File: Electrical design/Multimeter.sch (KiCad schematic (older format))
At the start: 31 parts

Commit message: Updated schematics.
Added speaker / buzzer, reset circuit (battery under-voltage lockout), changed battery charger IC.
Altered Vout circuit.
Added most resistor / capacitor values (those missing are either dependent on battery thermistor or ADC).
Updated to show "correct" op-amps.
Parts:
- removed C? (x7): CP1, symbol CP1
- removed Q?: Q_NMOS_DGS, symbol Q_NMOS_DGS
- removed Q?: Q_PMOS_DGS, symbol Q_PMOS_DGS
- added C106, C116, C119: 1u, my footprints:SMDuniversal_0603to1210_HandSoldering, symbol C
- added C108: 0.1u, my footprints:SMDuniversal_0603to1210_HandSoldering, symbol C
- added C109, C120, C121: 10u, my footprints:SMDuniversal_0603to1210_HandSoldering, symbol C
- added C112, C113, C118: 0.01u, my footprints:SMDuniversal_0603to1210_HandSoldering, symbol C
- added Q101: Q_PMOS_GSD, TO_SOT_Packages_SMD:SOT-23, symbol Q_PMOS_GSD
- added Q102: Q_NMOS_GSD, TO_SOT_Packages_SMD:SOT-23, symbol Q_NMOS_GSD
- added SP101: SPEAKER, Pin_Headers:Pin_Header_Straight_1x02, symbol SPEAKER
- added U103: BD4835, my footprints:VSOF5_HandSoldering, symbol BD4835
- C101, C102: renamed from C?; value C -> 18p; footprint (none) -> my footprints:SMDuniversal_0603to1210_HandSoldering
- C103, C104, C105: renamed from C?; value C -> 0.22u; footprint (none) -> my footprints:SMDuniversal_0603to1210_HandSoldering
- C107: renamed from C?; value C -> 1u; footprint (none) -> my footprints:SMDuniversal_0603to1210_HandSoldering
- C110, C117: renamed from C?; value C -> 0.1u; footprint (none) -> my footprints:SMDuniversal_0603to1210_HandSoldering
- C111: renamed from C?; value C -> 0.01u; footprint (none) -> my footprints:SMDuniversal_0603to1210_HandSoldering
- C114, C115: renamed from C?; footprint (none) -> my footprints:SMDuniversal_0603to1210_HandSoldering
- JP101: renamed from JP?; value Jumper_NO_Small -> BOOT0; footprint (none) -> Pin_Headers:Pin_Header_Straight_1x02
- P101: renamed from P?; footprint (none) -> Pin_Headers:Pin_Header_Straight_2x07
- P102: renamed from P?; footprint (none) -> Pin_Headers:Pin_Header_Straight_1x06
- R101, R102, R103: renamed from R?; value R -> 1k; footprint (none) -> my footprints:SMDuniversal_0603to1210_HandSoldering
- R104, R105: renamed from R?; value R -> 100k; footprint (none) -> my footprints:SMDuniversal_0603to1210_HandSoldering
- U101: renamed from U?; footprint LQFP64 -> Housings_QFP:LQFP-64_10x10mm_Pitch0.5mm
- U102: renamed from U?; footprint (none) -> my footprints:ILI9341_LCD_Breakout
- Y101: renamed from Y?; footprint (none) -> Crystals:Crystal_HC49-SD_SMD
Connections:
- net +3.3VA: now also C106.2, C112.2
- net +3V3: now also C108.1, C109.2, C120.2, C121.1, Q101.2 (S), U103.5 (VDD)
- net +Vref: now also C113.1, C116.1, C118.2, C119.2
- net GNDA: now also C106.1, C112.1, C113.2, C116.2, C118.1, C119.1, SP101.2
- net GNDD: now also C108.2, C109.1, C120.1, C121.2, Q102.2 (S), U103.2 (SUB), U103.4 (GND)
- net NRST: now also U103.1 (Vout)
- net PS_EN: now also Q102.1 (G)
- net at U101.22 (ADC1_IN6/COMP1_OUT/DAC2_OUT1/I2S1_MCK/SPI1_MISO/TIM13_CH1/TIM16_CH1/TIM3_CH1/TSC_G2_IO3/PA6): now also SP101.1
- net at U101.24 (PC4/ADC1_IN14/TIM13_CH1/TSC_G3_IO1/USART1_TX): now also R105.1, Q101.1 (G)
- net at U102.2 (GND): now also Q102.3 (D)
- net at U102.8 (LED): now also Q101.3 (D)
- no-connect marks 2 -> 1
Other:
- moved on the sheet: JP101, R104

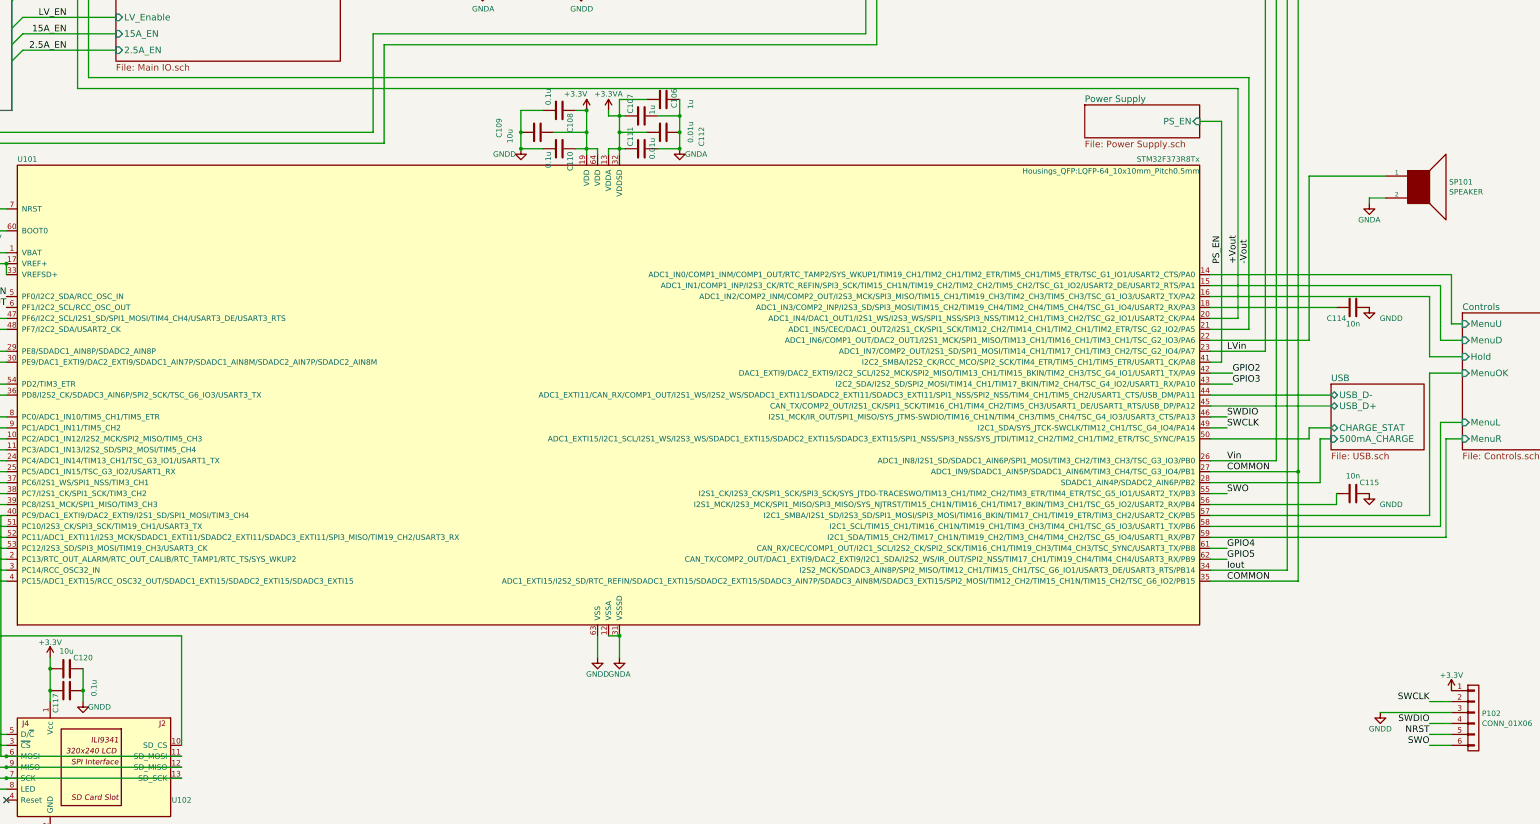
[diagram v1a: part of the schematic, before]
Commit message: Add battery voltage monitoring.
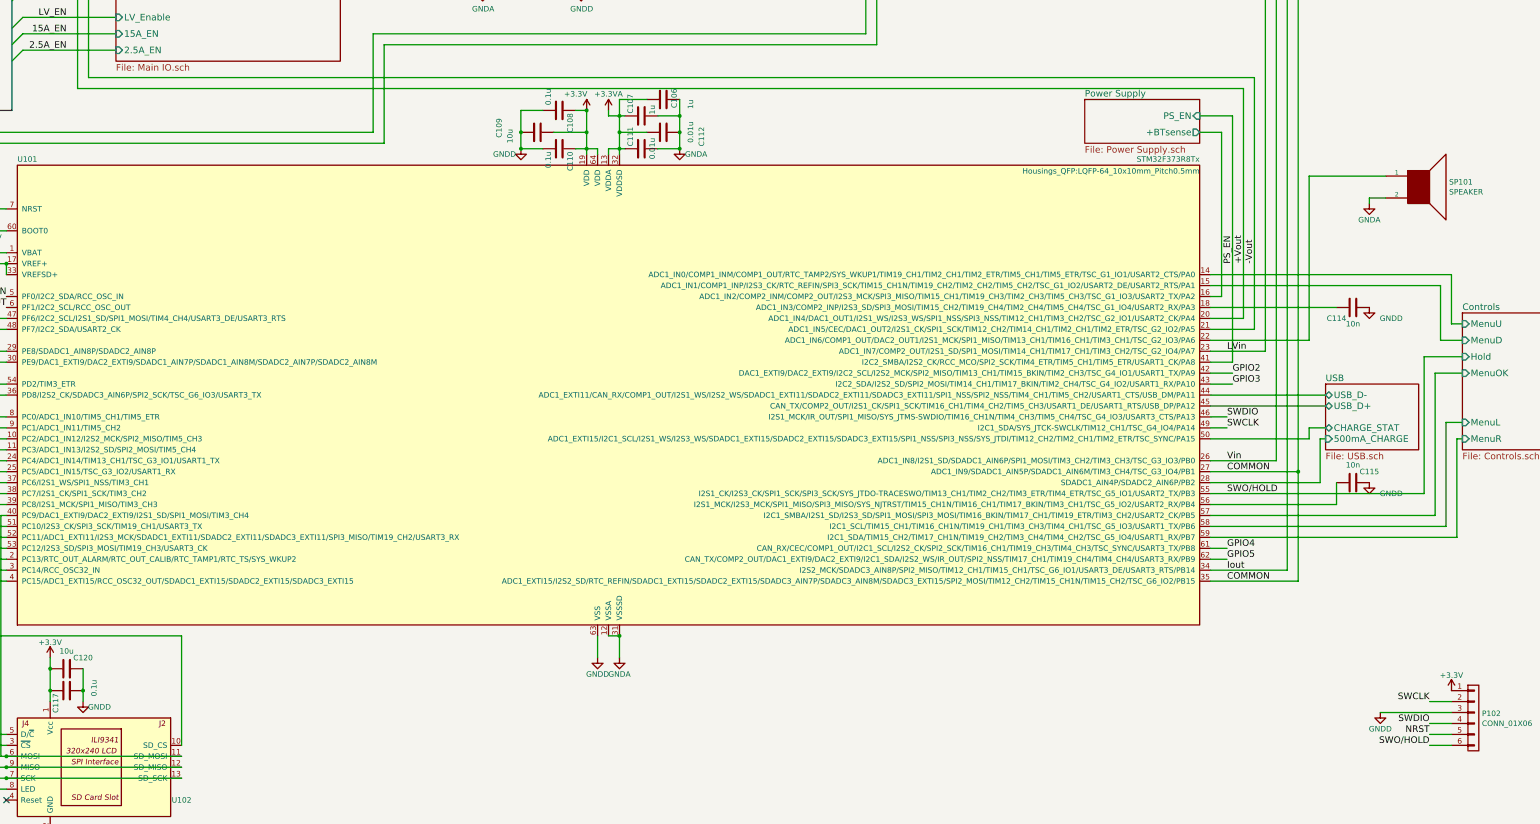
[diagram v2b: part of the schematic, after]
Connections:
- net Controls/Hold renamed Power Supply/+BTsense
- net SWO renamed SWO/HOLD
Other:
- moved on the sheet: C115

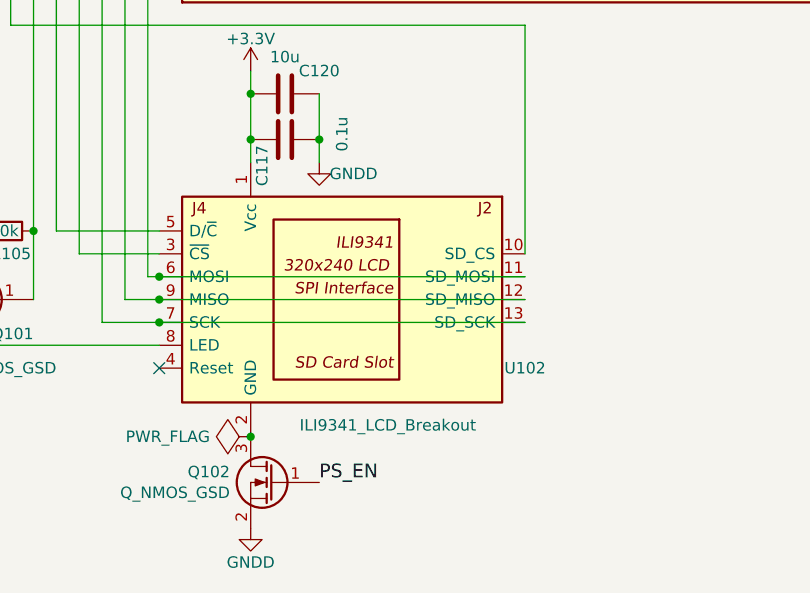
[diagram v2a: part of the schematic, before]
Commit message: Update External Design. Add battery sense capacitor. Update footprints.
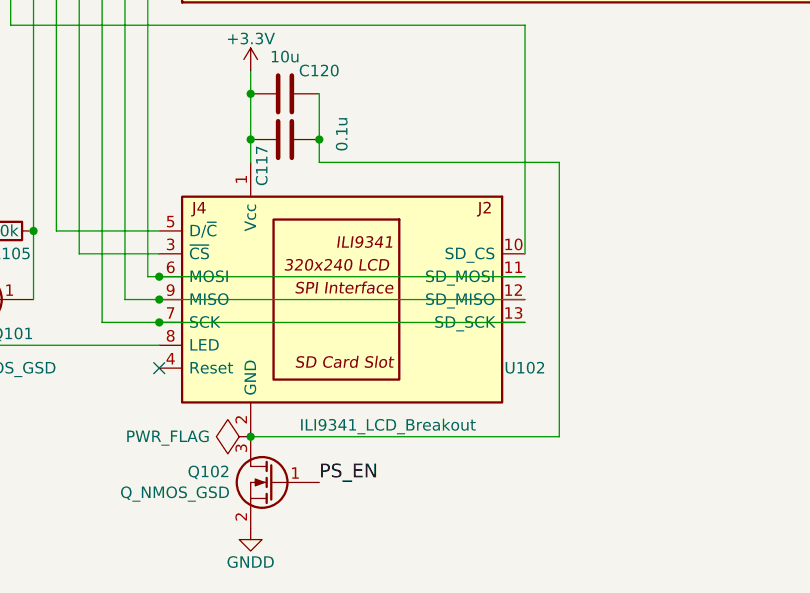
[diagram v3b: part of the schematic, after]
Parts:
- C101, C102, C103, C104, C105, C106, C107, C108, C110, C111, C112, C113, C114, C115, C116, C117, C118, C119: footprint my footprints:SMDuniversal_0603to1210_HandSoldering -> my footprints:SMDuniversal_0603to0805_HandSoldering
- C109, C120, C121: footprint my footprints:SMDuniversal_0603to1210_HandSoldering -> my footprints:SMDuniversal_0603to1206_HandSoldering
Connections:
- net GNDD: no longer C117.2, C120.1
- net at Q102.3 (D), U102.2 (GND): now also C117.2, C120.1
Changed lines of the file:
@@
 Sheet 1 5
 Title "Multimeter – Overview"
-Date ""
+Date "2016-06-22"
 Rev "0.5"
 Comp ""
@@
 F 0 "C111" H 7450 4250 50  0000 L CNN
 F 1 "0.01u" H 7550 4450 50  0000 L CNN
-F 2 "my footprints:SMDuniversal_0603to1210_HandSoldering" H 7688 4200 50  0001 C CNN
+F 2 "my footprints:SMDuniversal_0603to0805_HandSoldering" H 7688 4200 50  0001 C CNN
 F 3 "" H 7650 4350 50  0000 C CNN
 	1    7650 4350
@@
 F 0 "C110" H 6925 4450 50  0000 L CNN
 F 1 "0.1u" H 6925 4250 50  0000 L CNN
-F 2 "my footprints:SMDuniversal_0603to1210_HandSoldering" H 6938 4200 50  0001 C CNN
+F 2 "my footprints:SMDuniversal_0603to0805_HandSoldering" H 6938 4200 50  0001 C CNN
 F 3 "" H 6900 4350 50  0000 C CNN
 	1    6900 4350
@@
 F 0 "C107" H 7450 3950 50  0000 L CNN
 F 1 "1u" H 7550 4150 50  0000 L CNN
-F 2 "my footprints:SMDuniversal_0603to1210_HandSoldering" H 7688 3900 50  0001 C CNN
+F 2 "my footprints:SMDuniversal_0603to0805_HandSoldering" H 7688 3900 50  0001 C CNN
 F 3 "" H 7650 4050 50  0000 C CNN
 	1    7650 4050
@@
 F 0 "C115" V 14050 7550 50  0000 C CNN
 F 1 "10n" V 13989 7400 50  0000 C CNN
-F 2 "my footprints:SMDuniversal_0603to1210_HandSoldering" H 14188 7250 50  0001 C CNN
+F 2 "my footprints:SMDuniversal_0603to0805_HandSoldering" H 14188 7250 50  0001 C CNN
 F 3 "" H 14150 7400 50  0000 C CNN
 	1    14150 7400
@@
 F 0 "C114" V 14250 5650 50  0000 C CNN
 F 1 "10n" V 14300 5800 50  0000 C CNN
-F 2 "my footprints:SMDuniversal_0603to1210_HandSoldering" H 14188 5650 50  0001 C CNN
+F 2 "my footprints:SMDuniversal_0603to0805_HandSoldering" H 14188 5650 50  0001 C CNN
 F 3 "" H 14150 5800 50  0000 C CNN
 	1    14150 5800
@@
 F 0 "C102" H 1065 1246 50  0000 L CNN
 F 1 "18p" H 1065 1155 50  0000 L CNN
-F 2 "my footprints:SMDuniversal_0603to1210_HandSoldering" H 988 1050 50  0001 C CNN
+F 2 "my footprints:SMDuniversal_0603to0805_HandSoldering" H 988 1050 50  0001 C CNN
 F 3 "" H 950 1200 50  0000 C CNN
 	1    950  1200
@@
 F 0 "C101" H 1065 746 50  0000 L CNN
 F 1 "18p" H 1065 655 50  0000 L CNN
-F 2 "my footprints:SMDuniversal_0603to1210_HandSoldering" H 988 550 50  0001 C CNN
+F 2 "my footprints:SMDuniversal_0603to0805_HandSoldering" H 988 550 50  0001 C CNN
 F 3 "" H 950 700 50  0000 C CNN
 	1    950  700
@@
 F 0 "C117" H 2425 9400 50  0000 L CNN
 F 1 "0.1u" H 2300 9050 50  0000 L CNN
-F 2 "my footprints:SMDuniversal_0603to1210_HandSoldering" H 2438 9150 50  0001 C CNN
+F 2 "my footprints:SMDuniversal_0603to0805_HandSoldering" H 2438 9150 50  0001 C CNN
 F 3 "" H 2400 9300 50  0000 C CNN
 	1    2400 9300
 	0    -1   1    0
-$EndComp
-$Comp
-L GNDD #PWR018
-U 1 1 574E415A
-P 2550 9400
-F 0 "#PWR018" H 2550 9150 50  0001 C CNN
-F 1 "GNDD" H 2400 9350 50  0000 C CNN
-F 2 "" H 2550 9400 50  0000 C CNN
-F 3 "" H 2550 9400 50  0000 C CNN
-	1    2550 9400
-	-1   0    0    -1
 $EndComp
 Entry Wire Line
@@
 F 0 "C103" H 8350 2150 50  0000 L CNN
 F 1 "0.22u" H 8350 1950 50  0000 L CNN
-F 2 "my footprints:SMDuniversal_0603to1210_HandSoldering" H 8338 1900 50  0001 C CNN
+F 2 "my footprints:SMDuniversal_0603to0805_HandSoldering" H 8338 1900 50  0001 C CNN
 F 3 "" H 8300 2050 50  0000 C CNN
 	1    8300 2050
@@
 F 0 "C104" H 8750 2150 50  0000 L CNN
 F 1 "0.22u" H 8750 1950 50  0000 L CNN
-F 2 "my footprints:SMDuniversal_0603to1210_HandSoldering" H 8738 1900 50  0001 C CNN
+F 2 "my footprints:SMDuniversal_0603to0805_HandSoldering" H 8738 1900 50  0001 C CNN
 F 3 "" H 8700 2050 50  0000 C CNN
 	1    8700 2050
@@
 F 0 "C105" H 9150 2150 50  0000 L CNN
 F 1 "0.22u" H 9150 1950 50  0000 L CNN
-F 2 "my footprints:SMDuniversal_0603to1210_HandSoldering" H 9138 1900 50  0001 C CNN
+F 2 "my footprints:SMDuniversal_0603to0805_HandSoldering" H 9138 1900 50  0001 C CNN
 F 3 "" H 9100 2050 50  0000 C CNN
 	1    9100 2050
@@
 F 0 "C106" H 7750 4000 50  0000 L CNN
 F 1 "1u" H 7850 4150 50  0000 L CNN
-F 2 "my footprints:SMDuniversal_0603to1210_HandSoldering" H 7888 3750 50  0001 C CNN
+F 2 "my footprints:SMDuniversal_0603to0805_HandSoldering" H 7888 3750 50  0001 C CNN
 F 3 "" H 7850 3900 50  0000 C CNN
 	1    7850 3900
@@
 F 0 "C112" H 7800 4550 50  0000 L CNN
 F 1 "0.01u" H 7750 4450 50  0000 L CNN
-F 2 "my footprints:SMDuniversal_0603to1210_HandSoldering" H 7888 4050 50  0001 C CNN
+F 2 "my footprints:SMDuniversal_0603to0805_HandSoldering" H 7888 4050 50  0001 C CNN
 F 3 "" H 7850 4200 50  0000 C CNN
 	1    7850 4200
@@
 F 0 "C108" H 6925 4100 50  0000 L CNN
 F 1 "0.1u" H 6700 3900 50  0000 L CNN
-F 2 "my footprints:SMDuniversal_0603to1210_HandSoldering" H 6938 3850 50  0001 C CNN
+F 2 "my footprints:SMDuniversal_0603to0805_HandSoldering" H 6938 3850 50  0001 C CNN
 F 3 "" H 6900 4000 50  0000 C CNN
 	1    6900 4000
@@
 F 0 "C118" H 850 5450 50  0000 L CNN
 F 1 "0.01u" H 850 5650 50  0000 L CNN
-F 2 "my footprints:SMDuniversal_0603to1210_HandSoldering" H 988 5400 50  0001 C CNN
+F 2 "my footprints:SMDuniversal_0603to0805_HandSoldering" H 988 5400 50  0001 C CNN
 F 3 "" H 950 5550 50  0000 C CNN
 	1    950  5550
@@
 F 0 "C119" H 1050 5450 50  0000 L CNN
 F 1 "1u" H 1050 5650 50  0000 L CNN
-F 2 "my footprints:SMDuniversal_0603to1210_HandSoldering" H 1188 5400 50  0001 C CNN
+F 2 "my footprints:SMDuniversal_0603to0805_HandSoldering" H 1188 5400 50  0001 C CNN
 F 3 "" H 1150 5550 50  0000 C CNN
 	1    1150 5550
@@
 F 0 "C113" H 850 4950 50  0000 L CNN
 F 1 "0.01u" H 850 5150 50  0000 L CNN
-F 2 "my footprints:SMDuniversal_0603to1210_HandSoldering" H 988 4900 50  0001 C CNN
+F 2 "my footprints:SMDuniversal_0603to0805_HandSoldering" H 988 4900 50  0001 C CNN
 F 3 "" H 950 5050 50  0000 C CNN
 	1    950  5050
@@
 F 0 "C116" H 1050 4950 50  0000 L CNN
 F 1 "1u" H 1050 5150 50  0000 L CNN
-F 2 "my footprints:SMDuniversal_0603to1210_HandSoldering" H 1188 4900 50  0001 C CNN
+F 2 "my footprints:SMDuniversal_0603to0805_HandSoldering" H 1188 4900 50  0001 C CNN
 F 3 "" H 1150 5050 50  0000 C CNN
 	1    1150 5050
@@
 F 0 "C109" H 6650 4550 50  0000 L CNN
 F 1 "10u" H 6600 4450 50  0000 L CNN
-F 2 "my footprints:SMDuniversal_0603to1210_HandSoldering" H 6738 4050 50  0001 C CNN
+F 2 "my footprints:SMDuniversal_0603to1206_HandSoldering" H 6738 4050 50  0001 C CNN
 F 3 "" H 6700 4200 50  0000 C CNN
 	1    6700 4200
@@
 F 0 "C121" H 915 9896 50  0000 L CNN
 F 1 "10u" H 915 9805 50  0000 L CNN
-F 2 "my footprints:SMDuniversal_0603to1210_HandSoldering" H 838 9700 50  0001 C CNN
+F 2 "my footprints:SMDuniversal_0603to1206_HandSoldering" H 838 9700 50  0001 C CNN
 F 3 "" H 800 9850 50  0000 C CNN
 	1    800  9850
@@
 F 0 "C120" V 2300 9250 50  0000 C CNN
 F 1 "10u" V 2239 9100 50  0000 C CNN
-F 2 "my footprints:SMDuniversal_0603to1210_HandSoldering" H 2438 8950 50  0001 C CNN
+F 2 "my footprints:SMDuniversal_0603to1206_HandSoldering" H 2438 8950 50  0001 C CNN
 F 3 "" H 2400 9100 50  0000 C CNN
 	1    2400 9100
@@
 Wire Wire Line
 	12950 5700 12850 5700
+Wire Wire Line
+	2550 9400 3600 9400
+Wire Wire Line
+	3600 9400 3600 10600
+Wire Wire Line
+	3600 10600 2250 10600
 $EndSCHEMATC
